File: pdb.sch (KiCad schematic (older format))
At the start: 0 parts

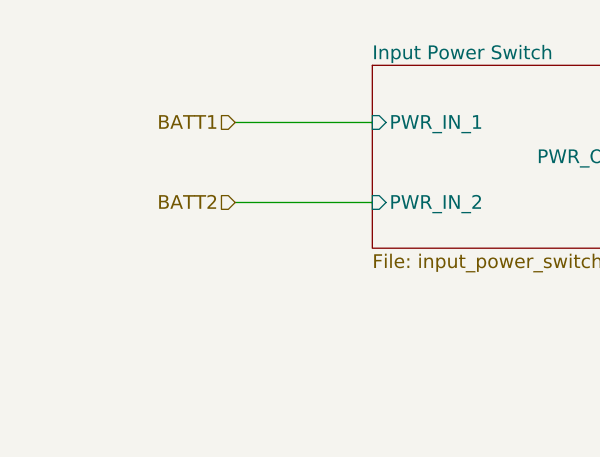
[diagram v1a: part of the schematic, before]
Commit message: add connectors for batteries
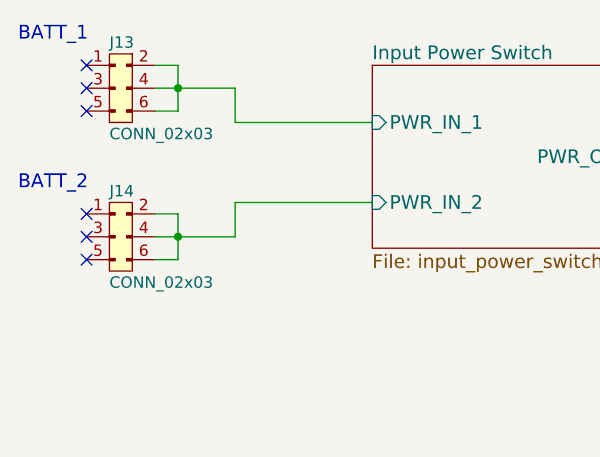
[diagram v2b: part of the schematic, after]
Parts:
- added J13, J14: CONN_02x03, symbol CONN_02x03
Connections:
- new net Input Power Switch/PWR_IN_1: J13.2, J13.4, J13.6
- new net Input Power Switch/PWR_IN_2: J14.2, J14.4, J14.6
- no-connect marks 0 -> 6
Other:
- note added: "BATT_1"
- note added: "BATT_2"
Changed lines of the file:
@@
 Wire Wire Line
 	7850 4400 8300 4400
-Text HLabel 1650 3050 0    60   Input ~ 0
-BATT1
-Wire Wire Line
-	1650 3050 2250 3050
-Text HLabel 1650 3400 0    60   Input ~ 0
-BATT2
-Wire Wire Line
-	1650 3400 2250 3400
 $Comp
 L GND #PWR01
@@
 Wire Wire Line
 	2600 5800 2600 5950
+$Comp
+L CONN_02x03 J14
+U 1 1 59628CF7
+P 1200 3450
+F 0 "J14" H 1100 3550 50  0000 L CNN
+F 1 "CONN_02x03" H 1100 3150 50  0000 L CNN
+F 2 "" H 1200 3450 50  0001 C CNN
+F 3 "" H 1200 3450 50  0001 C CNN
+	1    1200 3450
+	1    0    0    -1
+$EndComp
+$Comp
+L CONN_02x03 J13
+U 1 1 59628D6F
+P 1200 2800
+F 0 "J13" H 1100 2900 50  0000 L CNN
+F 1 "CONN_02x03" H 1100 2500 50  0000 L CNN
+F 2 "" H 1200 2800 50  0001 C CNN
+F 3 "" H 1200 2800 50  0001 C CNN
+	1    1200 2800
+	1    0    0    -1
+$EndComp
+Wire Wire Line
+	1300 2800 1400 2800
+Wire Wire Line
+	1400 2800 1400 3000
+Wire Wire Line
+	1400 3000 1300 3000
+Wire Wire Line
+	1300 2900 1650 2900
+Connection ~ 1400 2900
+Wire Wire Line
+	1650 2900 1650 3050
+Wire Wire Line
+	1300 3650 1400 3650
+Wire Wire Line
+	1400 3650 1400 3450
+Wire Wire Line
+	1400 3450 1300 3450
+Wire Wire Line
+	1650 3550 1300 3550
+Connection ~ 1400 3550
+Wire Wire Line
+	1650 3400 1650 3550
+NoConn ~ 1000 2800
+NoConn ~ 1000 2900
+NoConn ~ 1000 3000
+NoConn ~ 1000 3450
+NoConn ~ 1000 3550
+NoConn ~ 1000 3650
+Text Notes 700  2700 0    60   ~ 0
+BATT_1
+Text Notes 700  3350 0    60   ~ 0
+BATT_2
+Wire Wire Line
+	2250 3400 1650 3400
+Wire Wire Line
+	1650 3050 2250 3050
 $EndSCHEMATC

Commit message: assign footprints to components
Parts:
- J13, J14: footprint (none) -> Connectors_Molex:Molex_MegaFit_2x03x5.70mm_Straight
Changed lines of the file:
@@
 F 0 "J14" H 1100 3550 50  0000 L CNN
 F 1 "CONN_02x03" H 1100 3150 50  0000 L CNN
-F 2 "" H 1200 3450 50  0001 C CNN
+F 2 "Connectors_Molex:Molex_MegaFit_2x03x5.70mm_Straight" H 1200 3450 50  0001 C CNN
 F 3 "" H 1200 3450 50  0001 C CNN
 	1    1200 3450
@@
 F 0 "J13" H 1100 2900 50  0000 L CNN
 F 1 "CONN_02x03" H 1100 2500 50  0000 L CNN
-F 2 "" H 1200 2800 50  0001 C CNN
+F 2 "Connectors_Molex:Molex_MegaFit_2x03x5.70mm_Straight" H 1200 2800 50  0001 C CNN
 F 3 "" H 1200 2800 50  0001 C CNN
 	1    1200 2800
